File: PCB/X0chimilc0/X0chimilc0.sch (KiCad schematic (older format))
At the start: 0 parts

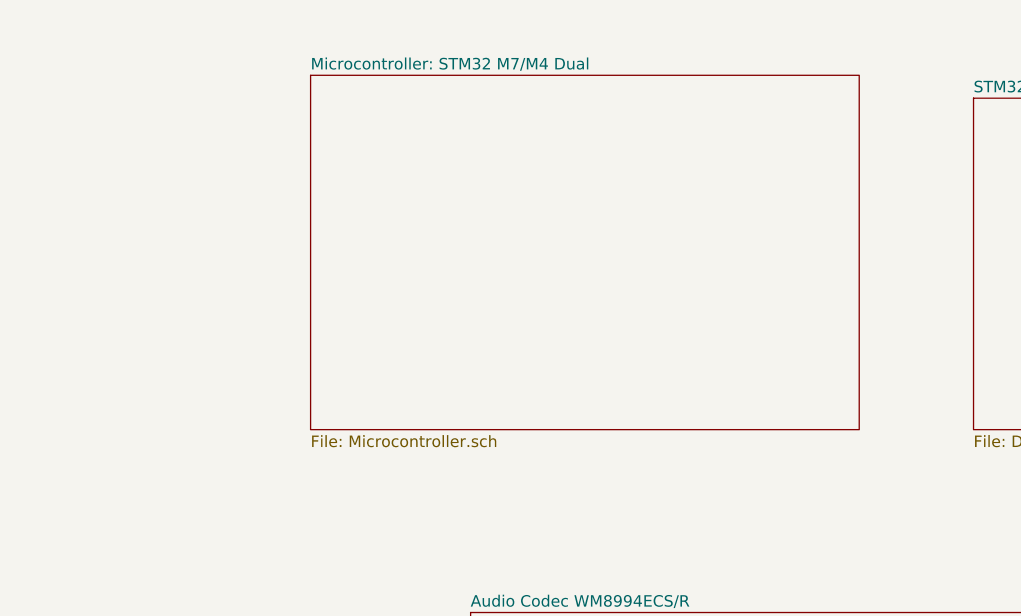
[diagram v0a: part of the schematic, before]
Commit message: PCB Mockup
Made components for DAC/MCU/FPGA/Connectors, mocked things up as PCB, going to be crazy.
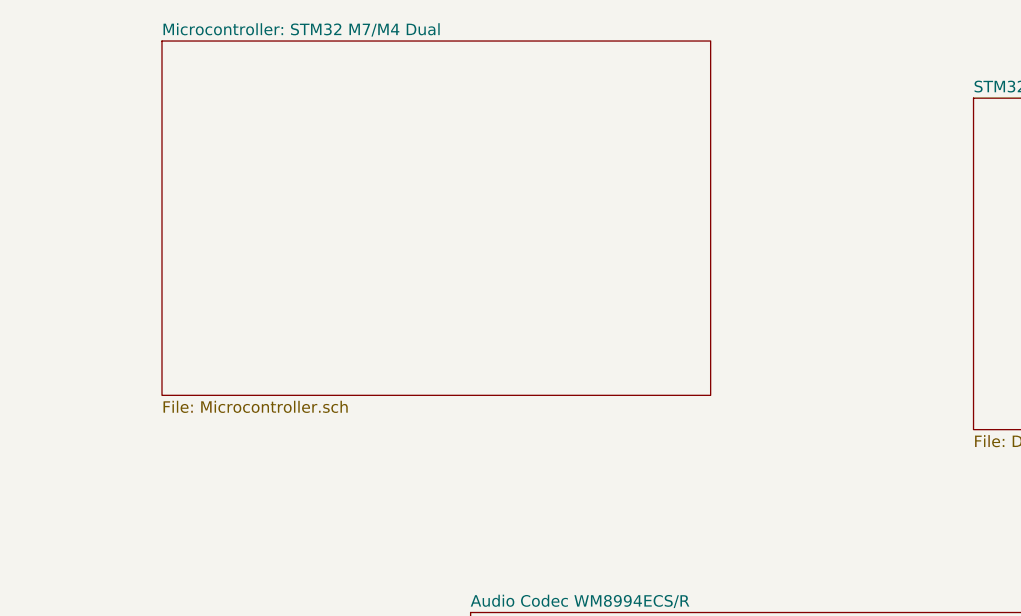
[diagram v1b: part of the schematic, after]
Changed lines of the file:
@@
 $EndSheet
 $Sheet
-S 5750 1200 2400 1550
+S 5100 1050 2400 1550
 U 5E2ACBAE
 F0 "Microcontroller: STM32 M7/M4 Dual" 50

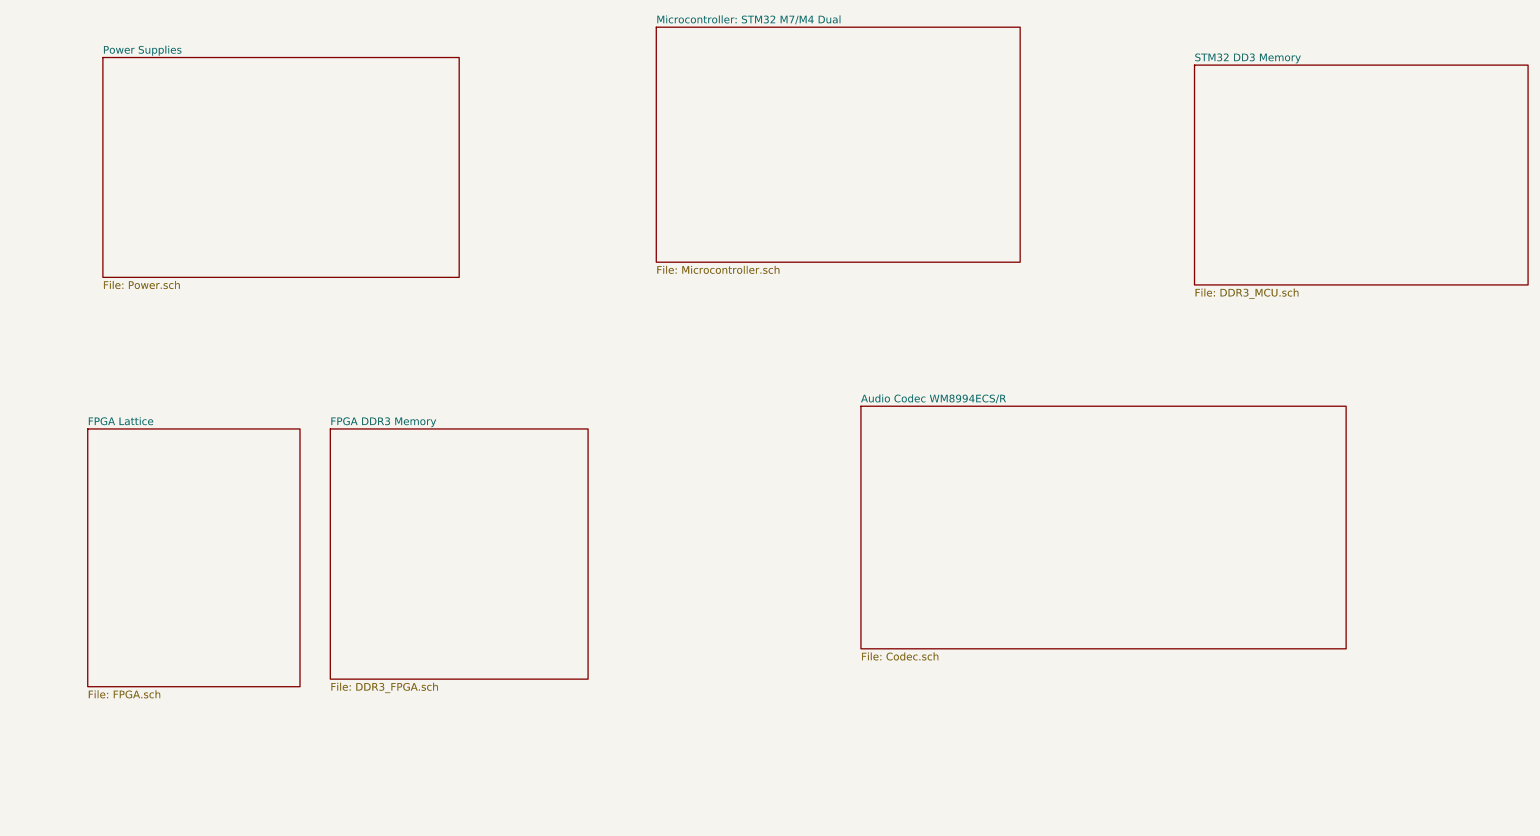
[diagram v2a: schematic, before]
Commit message: MCU Power
MCU power schematic completed, working on other MCU part and Codec.
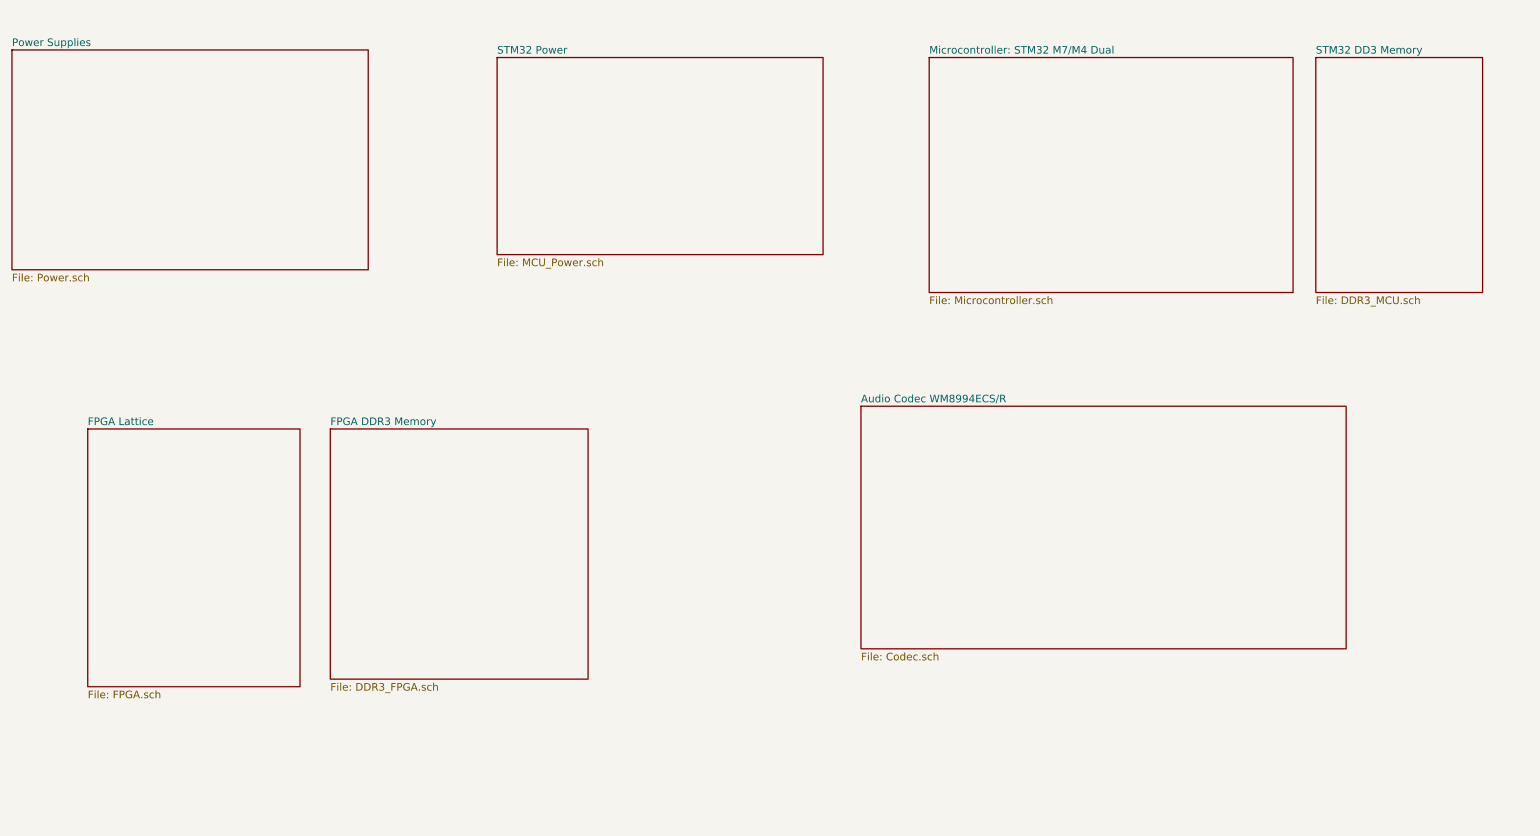
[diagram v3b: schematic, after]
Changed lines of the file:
@@
 $Descr A4 11693 8268
 encoding utf-8
-Sheet 1 7
+Sheet 1 8
 Title ""
 Date ""
@@
 $EndDescr
 $Sheet
-S 1450 1250 2350 1450
+S 850  1200 2350 1450
 U 5E2ACA94
 F0 "Power Supplies" 50
@@
 $EndSheet
 $Sheet
-S 5100 1050 2400 1550
+S 6900 1250 2400 1550
 U 5E2ACBAE
 F0 "Microcontroller: STM32 M7/M4 Dual" 50
@@
 $EndSheet
 $Sheet
-S 8650 1300 2200 1450
+S 9450 1250 1100 1550
 U 5E2AD524
 F0 "STM32 DD3 Memory" 50
@@
 F1 "Codec.sch" 50
 $EndSheet
+$Sheet
+S 4050 1250 2150 1300
+U 5E02C3CE
+F0 "STM32 Power " 50
+F1 "MCU_Power.sch" 50
+$EndSheet
 $EndSCHEMATC

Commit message: USB
USB C page of schematics first pass complete
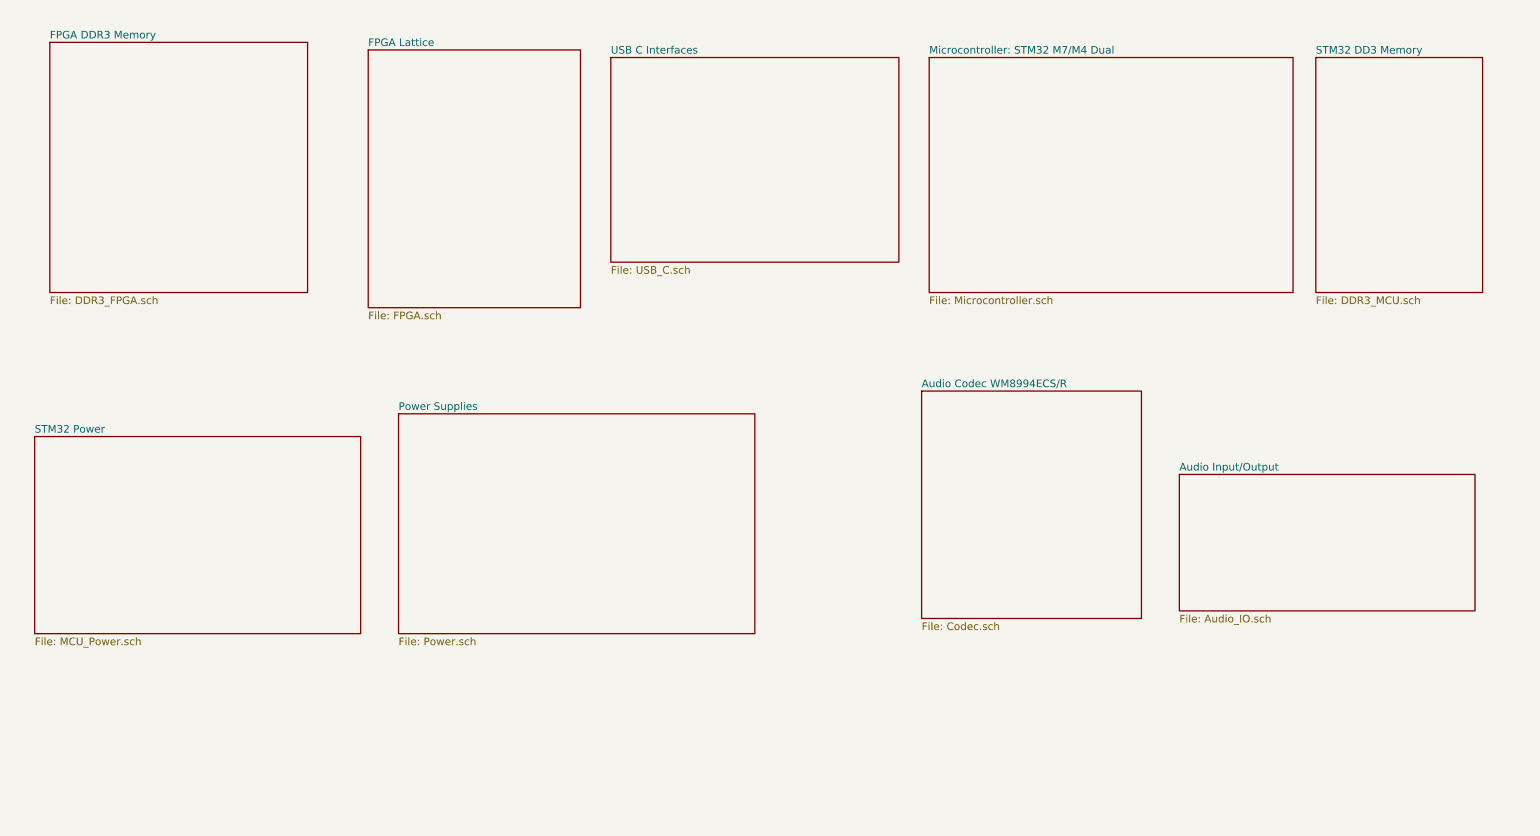
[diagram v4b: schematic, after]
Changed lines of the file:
@@
 $Descr A4 11693 8268
 encoding utf-8
-Sheet 1 8
+Sheet 1 10
 Title ""
 Date ""
@@
 $EndDescr
 $Sheet
-S 850  1200 2350 1450
+S 3400 3600 2350 1450
 U 5E2ACA94
 F0 "Power Supplies" 50
@@
 $EndSheet
 $Sheet
-S 1350 3700 1400 1700
+S 3200 1200 1400 1700
 U 5E2ACD97
 F0 "FPGA Lattice" 50
@@
 $EndSheet
 $Sheet
-S 2950 3700 1700 1650
+S 1100 1150 1700 1650
 U 5E2AD622
 F0 "FPGA DDR3 Memory" 50
@@
 $EndSheet
 $Sheet
-S 6450 3550 3200 1600
+S 6850 3450 1450 1500
 U 5E30BDF7
 F0 "Audio Codec WM8994ECS/R" 50
@@
 $EndSheet
 $Sheet
-S 4050 1250 2150 1300
+S 1000 3750 2150 1300
 U 5E02C3CE
 F0 "STM32 Power " 50
 F1 "MCU_Power.sch" 50
 $EndSheet
+$Sheet
+S 8550 4000 1950 900
+U 5E1A79E6
+F0 "Audio Input/Output" 50
+F1 "Audio_IO.sch" 50
+$EndSheet
+$Sheet
+S 4800 1250 1900 1350
+U 5DF40455
+F0 "USB C Interfaces" 50
+F1 "USB_C.sch" 50
+$EndSheet
 $EndSCHEMATC

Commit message: USB C DDR3L MCU
more with MCU and USB C and DDR3L
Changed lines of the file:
@@
 $Descr A4 11693 8268
 encoding utf-8
-Sheet 1 10
+Sheet 1 11
 Title ""
 Date ""
@@
 Comment4 ""
 $EndDescr
-$Sheet
-S 3400 3600 2350 1450
-U 5E2ACA94
-F0 "Power Supplies" 50
-F1 "Power.sch" 50
-$EndSheet
 $Sheet
 S 6900 1250 2400 1550
@@
 $EndSheet
 $Sheet
-S 6850 3450 1450 1500
+S 7050 4700 1450 1500
 U 5E30BDF7
 F0 "Audio Codec WM8994ECS/R" 50
@@
 $EndSheet
 $Sheet
-S 1000 3750 2150 1300
+S 6850 3100 2150 1300
 U 5E02C3CE
 F0 "STM32 Power " 50
@@
 $EndSheet
 $Sheet
-S 8550 4000 1950 900
+S 8750 5250 1950 900
 U 5E1A79E6
 F0 "Audio Input/Output" 50
@@
 F1 "USB_C.sch" 50
 $EndSheet
+$Sheet
+S 2550 3800 1400 1450
+U 5EA384BF
+F0 "FPGA Power Supply" 50
+F1 "FPGA_Power.sch" 50
+$EndSheet
+$Sheet
+S 4900 3150 1700 1150
+U 5E2ACA94
+F0 "Power Supplies" 50
+F1 "Power.sch" 50
+$EndSheet
 $EndSCHEMATC

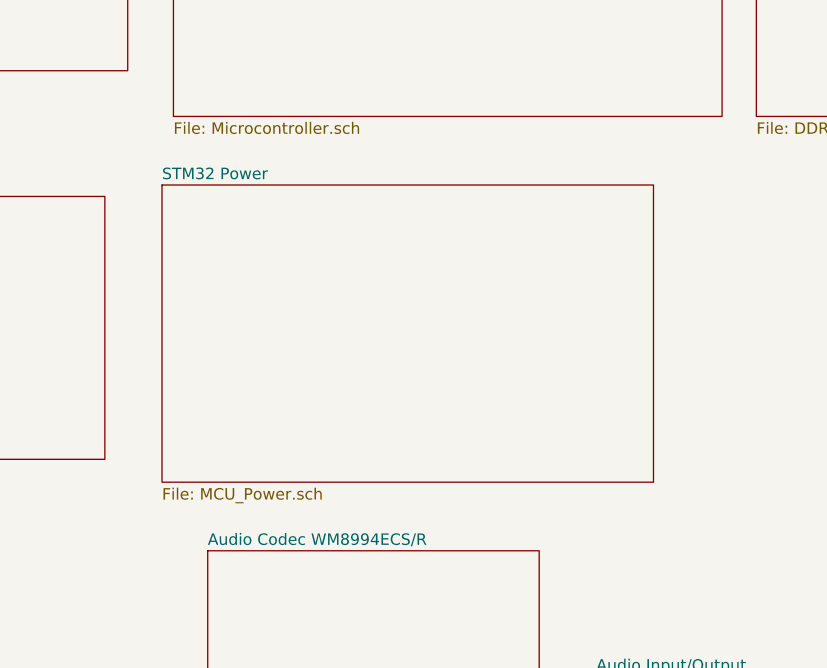
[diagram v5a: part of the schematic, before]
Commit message: Power Supply
Worked on power supply design adn schematic, still need a few more rails.
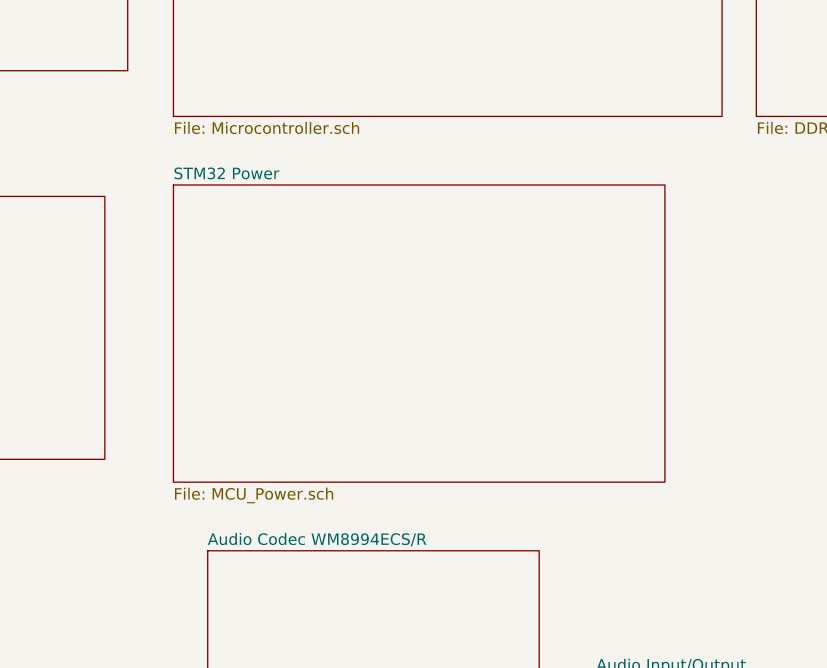
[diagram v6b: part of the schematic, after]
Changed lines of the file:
@@
 $EndSheet
 $Sheet
-S 6850 3100 2150 1300
+S 6900 3100 2150 1300
 U 5E02C3CE
 F0 "STM32 Power " 50
